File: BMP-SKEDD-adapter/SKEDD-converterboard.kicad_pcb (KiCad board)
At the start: 2 copper layers, 22.9 x 16.5 mm, 4 parts, among them J1 Conn_ARM_JTAG_SWD_10, J2 UART_HostSide, J3 Jitter_Debug_HostSide, J4 Conn_01x02_Pin

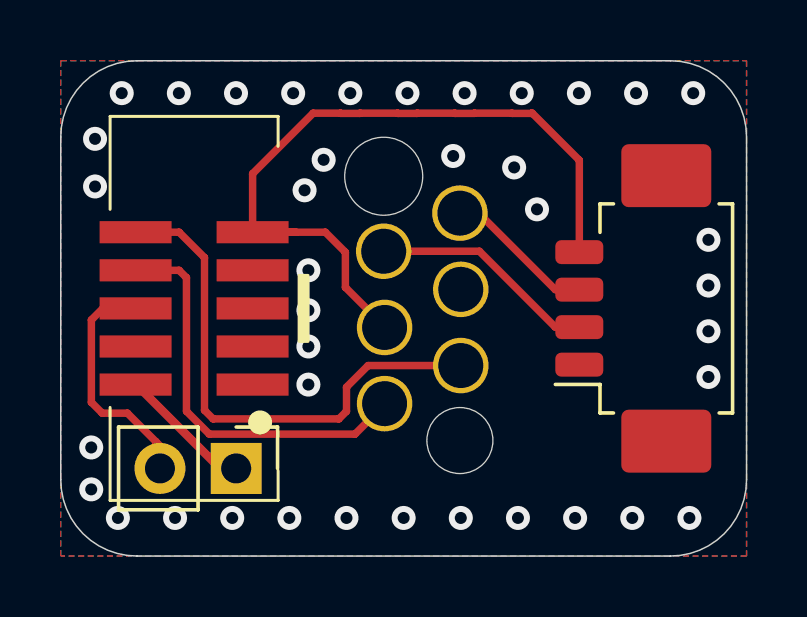
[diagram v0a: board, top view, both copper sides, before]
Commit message: Add Logos back with schematic symbol. Reverse SWO/RST connector
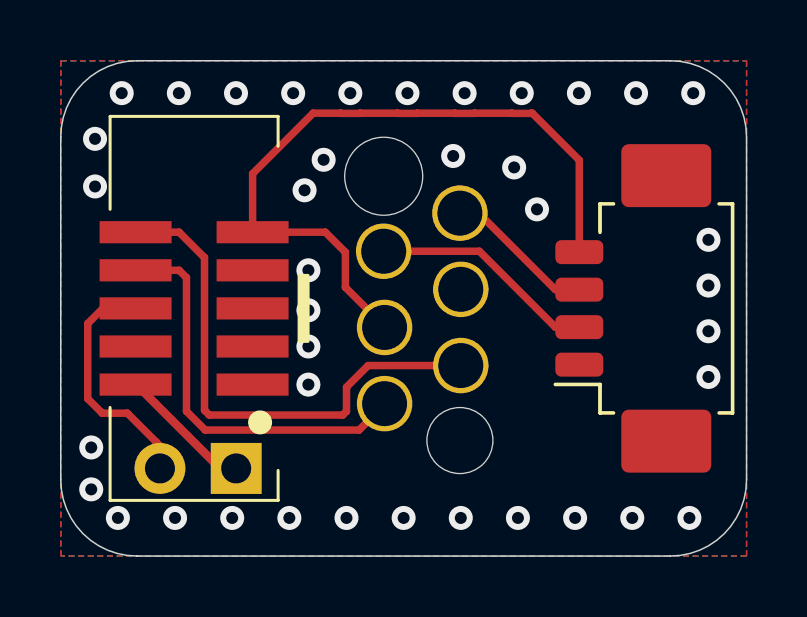
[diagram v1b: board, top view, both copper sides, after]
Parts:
- added LOGO1: LOGO, Jitter_Logos:Jitter-mini, B.Cu at (165.5, 112.7)
- added LOGO2: LOGO, Jitter_Logos:JitterLogo, B.Cu at (151.4, 102.4)
- J4: moved to B.Cu
- turned J4 to 90 degrees
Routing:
- net +3.3V: track 25.3 -> 23.8 mm
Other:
- board text added: "BMP REDFIT Adapter"
- board text removed: "DEBUGGER"
